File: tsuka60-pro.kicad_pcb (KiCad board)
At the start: 2 copper layers, 285 x 94.6 mm, 177 parts, among them J1 USB_C_Receptacle_USB2.0, J2 Conn_01x04_MountingPin, SW1 SW_Reset, U1 ATmega32U4-M, U2 SRV05-4, Y1 16MHz

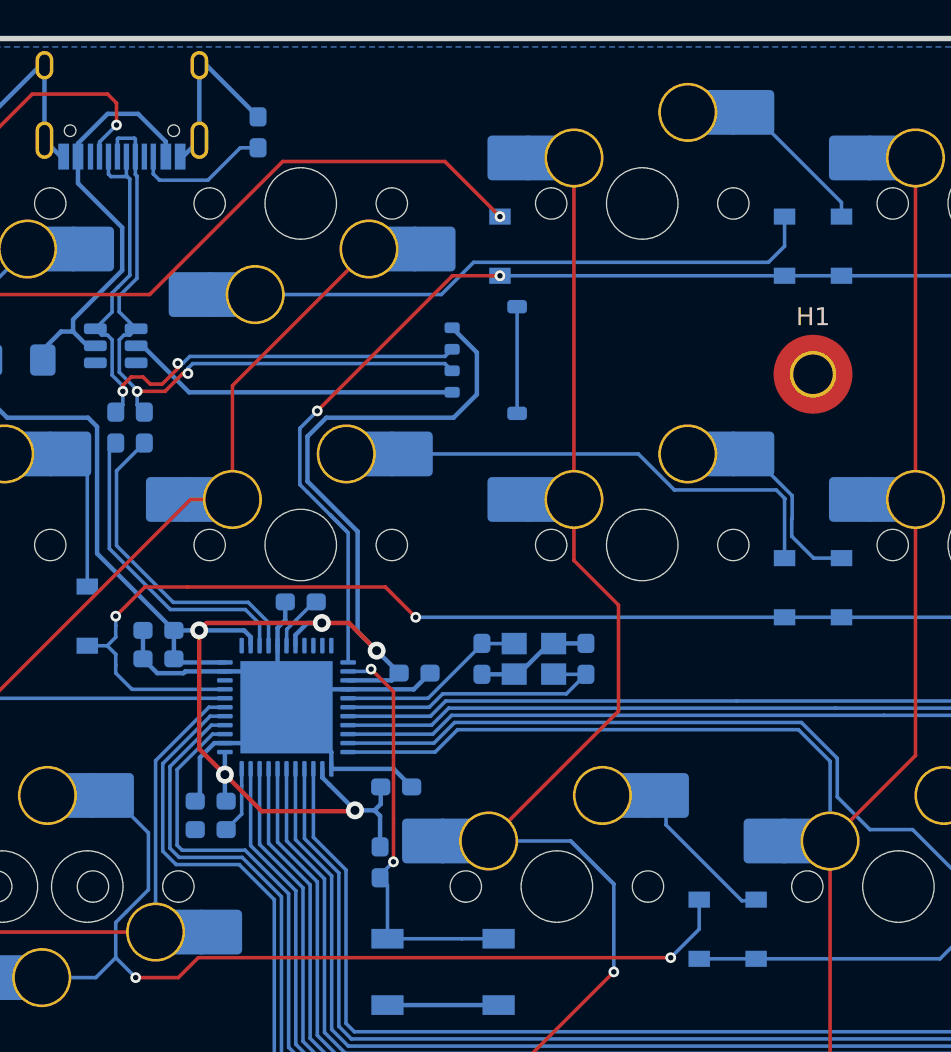
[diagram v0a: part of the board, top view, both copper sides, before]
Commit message: SIP socket placement
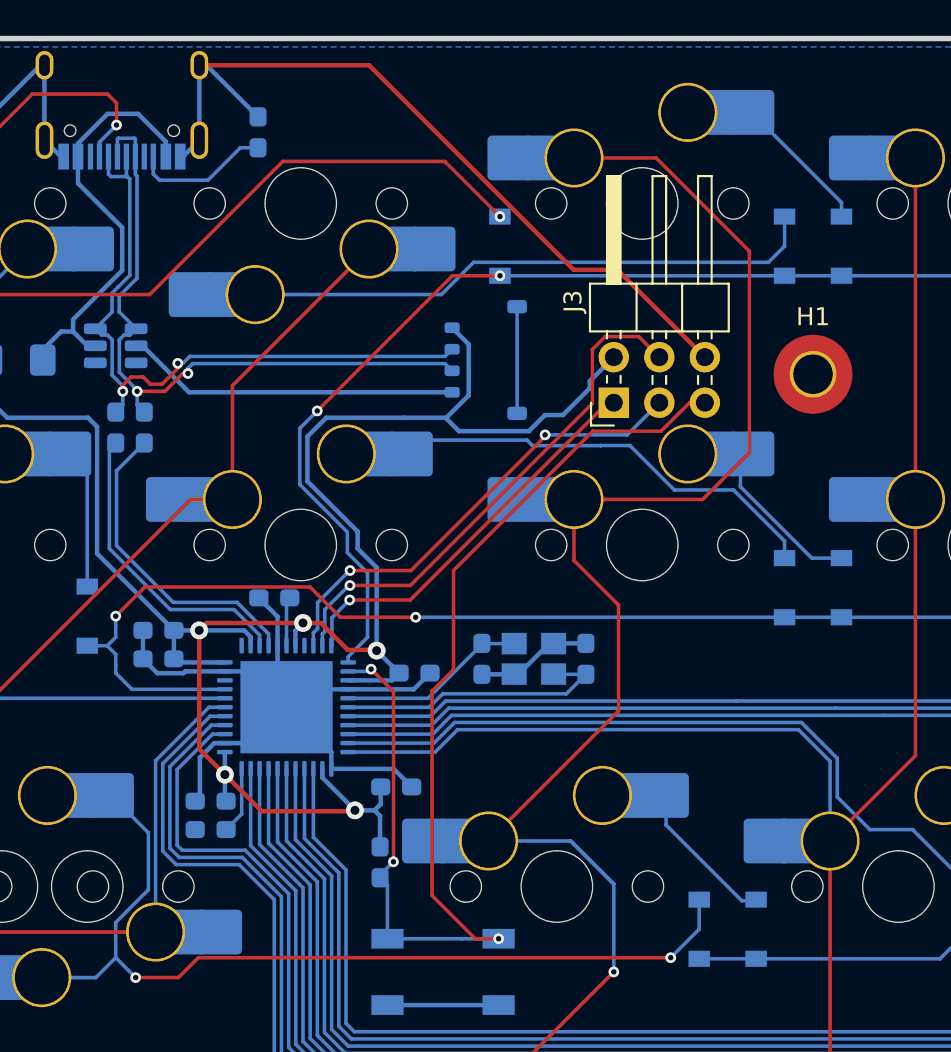
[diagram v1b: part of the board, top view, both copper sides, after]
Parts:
- added J3: AVR-ISP-6, Connector_PinHeader_2.54mm:PinHeader_2x03_P2.54mm_Horizontal, F.Cu at (109.5, 100.0)
- moved C3 1.49 mm to (90.6, 110.9)
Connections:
- U1 pad 10: unconnected-(U1-Pad10) -> MOSI
- U1 pad 11: unconnected-(U1-Pad11) -> MISO
- U1 pad 9: unconnected-(U1-Pad9) -> SCK
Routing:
- net RESET: track 23.6 -> 64.8 mm, vias 2 -> 3
- net GND: track 95.2 -> 130.6 mm
- net MOSI: track 0.00 -> 29.3 mm, vias 0 -> 1
- net SCK: track 0.00 -> 26.2 mm, vias 0 -> 2
- net MISO: track 0.00 -> 22.3 mm, vias 0 -> 1
- net COL2: track 131.7 -> 146.7 mm
- net +5V: track 104.9 -> 115.0 mm
- net Net-(D17-Pad2): track 25.3 -> 24.5 mm
- net Net-(D18-Pad2): track 8.82 -> 9.37 mm

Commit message: Relocate ISP header, retrace
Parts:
- moved D17 19.0 mm to (100.0, 110.3)
- moved D18 3.17 mm to (119.1, 110.3)
- moved J3 1.59 mm to (109.5, 98.4)
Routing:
- net Net-(D17-Pad2): track 24.5 -> 6.58 mm
- net Net-(D18-Pad2): track 9.37 -> 6.58 mm
- net MOSI: track 29.3 -> 30.9 mm
- net MISO: track 22.3 -> 23.6 mm
- net +5V: track 115.0 -> 113.7 mm
- net RESET: track 64.8 -> 65.5 mm
- net GND: track 130.6 -> 129.9 mm
- net SCK: track 26.2 -> 26.9 mm

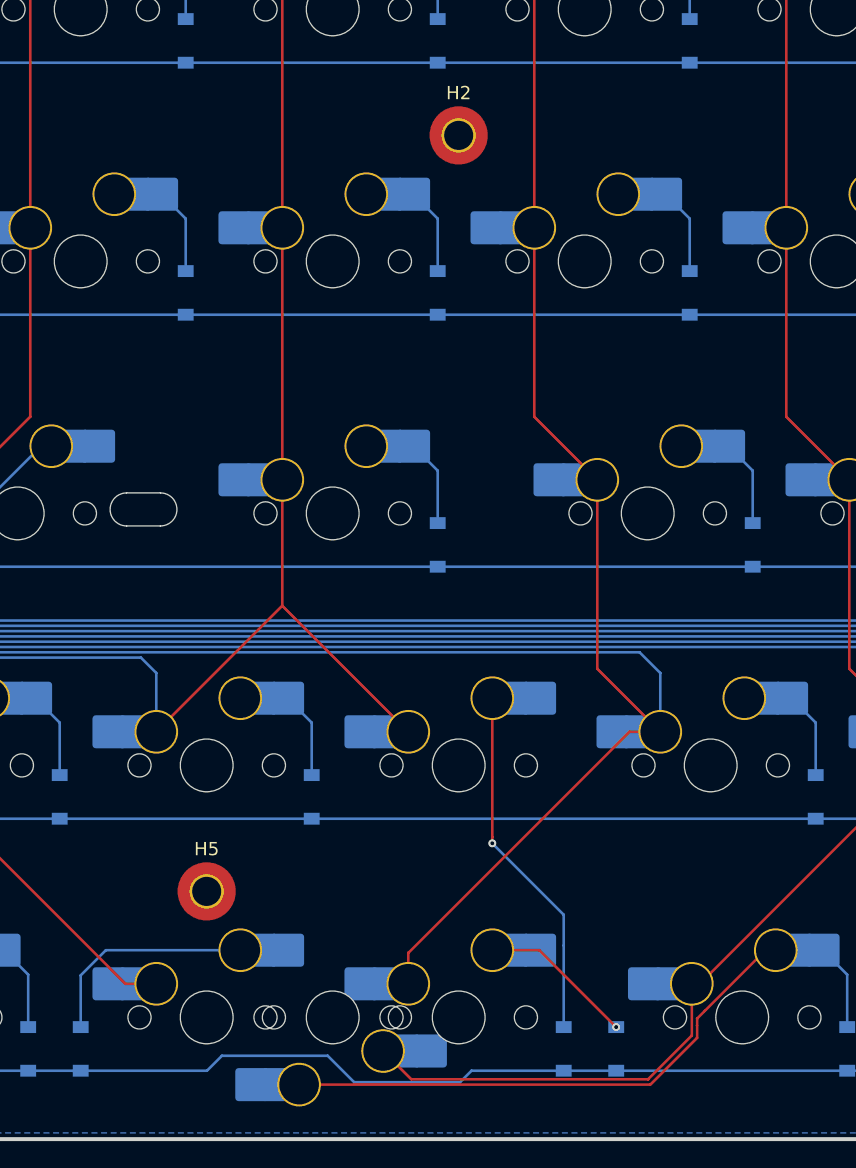
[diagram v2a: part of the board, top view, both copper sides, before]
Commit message: Add 2u stab, relocate mounting holes
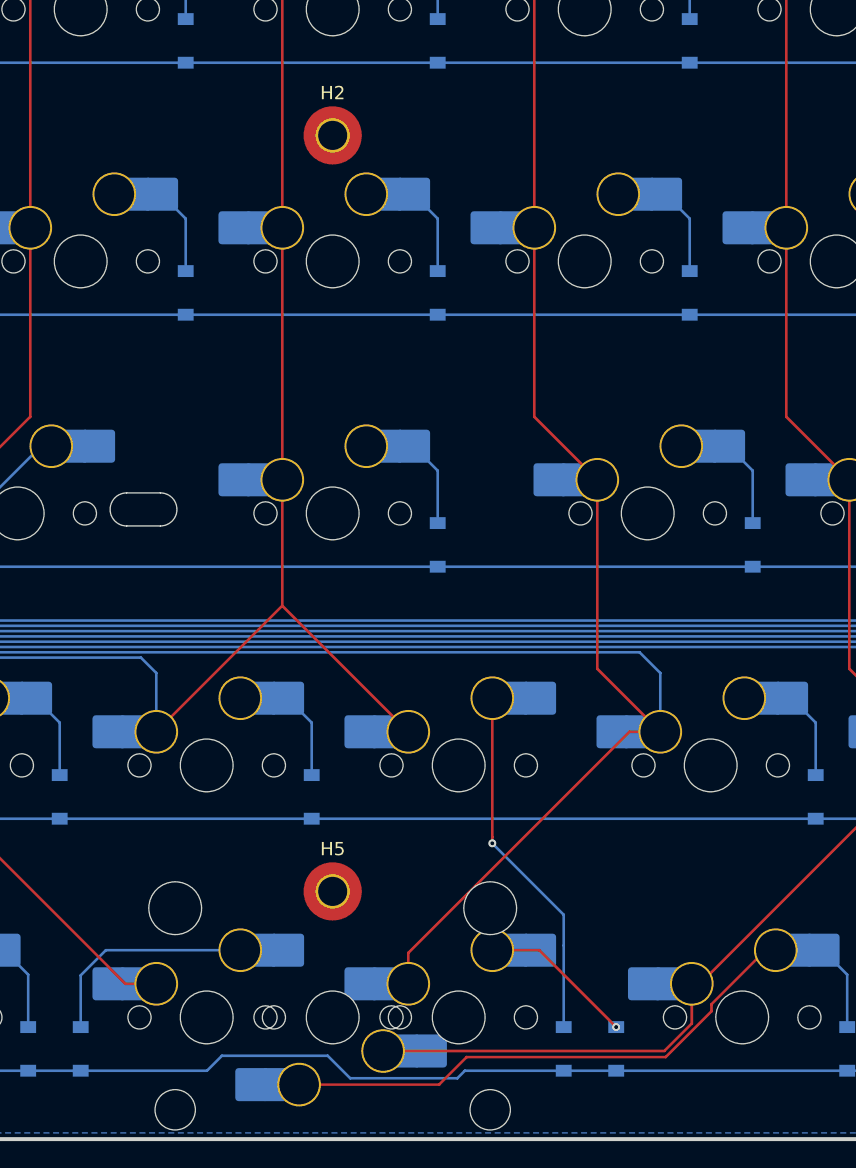
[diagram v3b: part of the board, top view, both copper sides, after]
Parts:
- added S2: MX_stab, marbastlib-mx:STAB_MX_2u, F.Cu at (206.4, 165.1)
- moved H2 9.53 mm to (206.4, 98.4)
- moved H5 9.53 mm to (206.4, 155.6)
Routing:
- net COL9: track 296.4 -> 294.1 mm
- net 70_2: track 47.7 -> 47.1 mm

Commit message: Reposition and retrace ISP footprint, update BOM and production files
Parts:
- moved J3 32.8 mm to (141.9, 93.5), turned to 0 degrees
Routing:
- net GND: track 129.9 -> 214.3 mm, vias 0 -> 2
- net +5V: track 113.7 -> 149.0 mm
- net MISO: track 23.6 -> 58.6 mm, vias 1 -> 3
- net SCK: track 26.9 -> 60.0 mm
- net MOSI: track 30.9 -> 62.6 mm, vias 1 -> 2
- net RESET: track 65.5 -> 96.4 mm, vias 3 -> 4
- net ROW0: track 258.1 -> 259.5 mm
- added copper zone on F.Cu, net (none)
